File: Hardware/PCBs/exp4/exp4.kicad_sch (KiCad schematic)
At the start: 10 parts, among them J1 Conn_01x06_Female, J2 Conn_01x05_Female, J3 Conn_01x05_Female, J4 Conn_01x05_Female, U1 7486, U2 7486

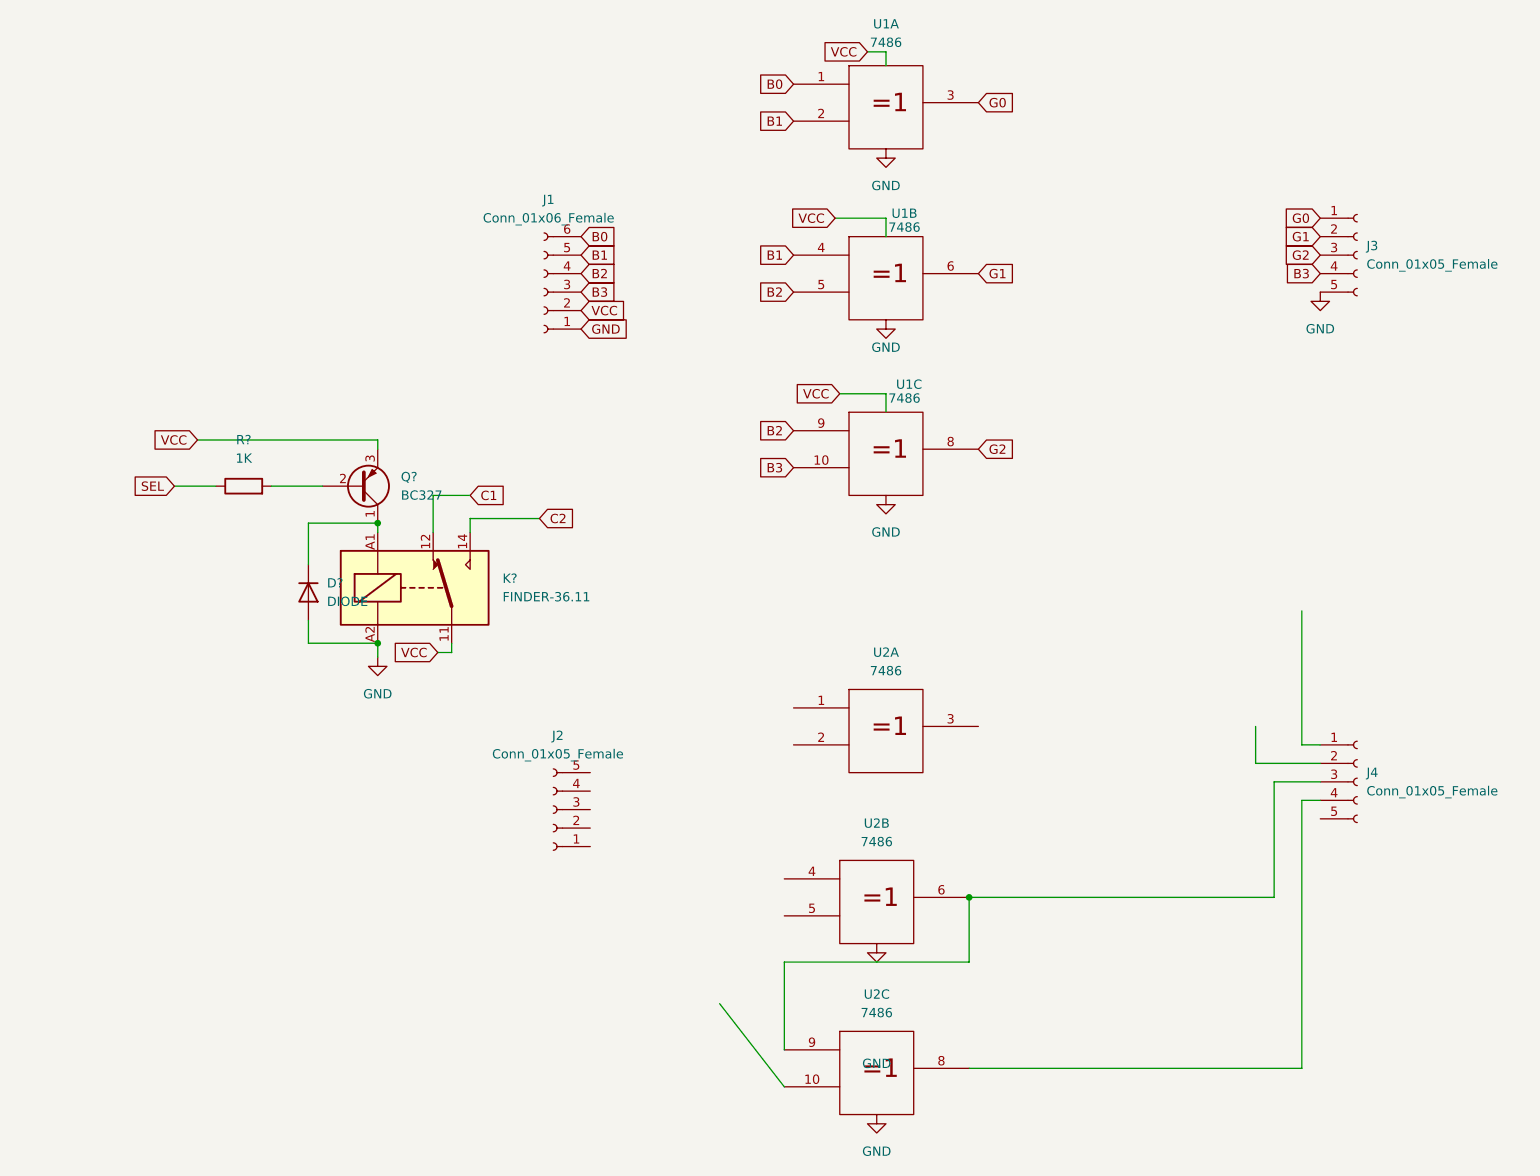
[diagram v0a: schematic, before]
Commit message: Several PCBs updated
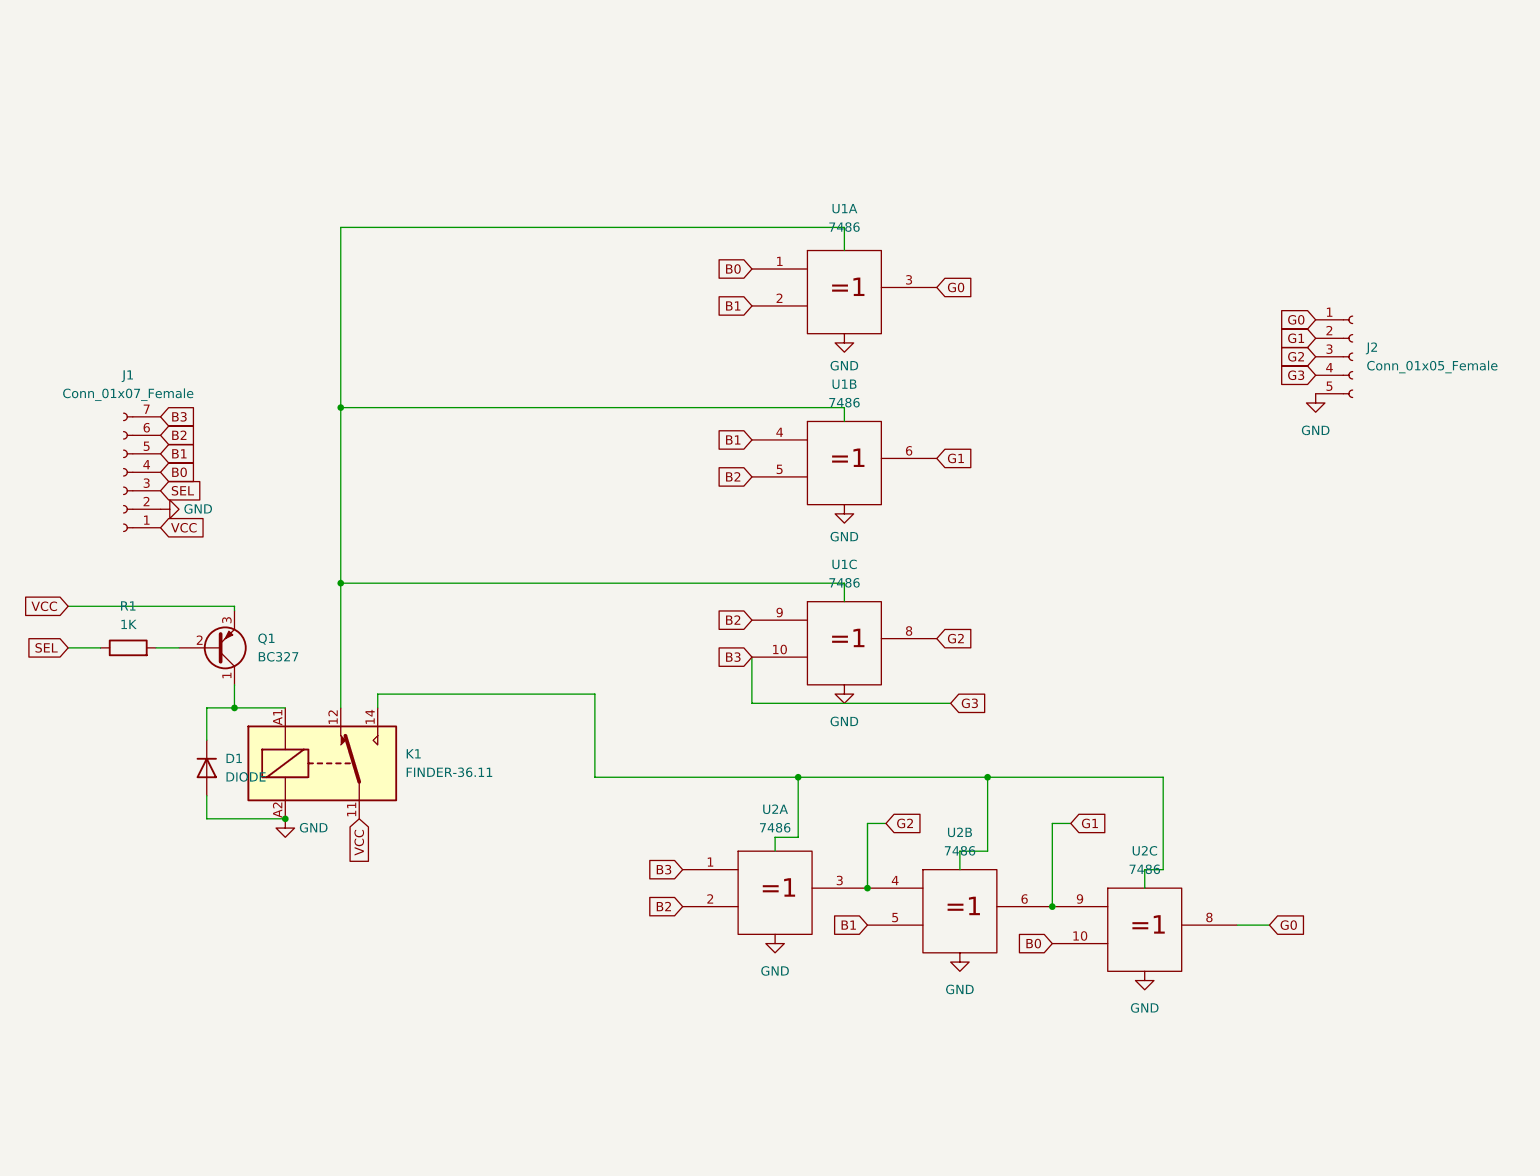
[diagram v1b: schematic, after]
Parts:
- removed D?: DIODE, Diode_SMD:D_MiniMELF, symbol Simulation_SPICE:DIODE
- removed J1: Conn_01x06_Female, Connector_JST:JST_EH_S6B-EH_1x06_P2.50mm_Horizontal, symbol Connector:Conn_01x06_Female
- removed J3, J4: Conn_01x05_Female, Connector_JST:JST_EH_S5B-EH_1x05_P2.50mm_Horizontal, symbol Connector:Conn_01x05_Female
- removed K?: FINDER-36.11, Relay_THT:Relay_SPDT_Finder_36.11, symbol Relay:FINDER-36.11
- removed Q?: BC327, Package_TO_SOT_THT:TO-92_Inline, symbol Transistor_BJT:BC327
- removed R?: 1K, Resistor_THT:R_Axial_DIN0207_L6.3mm_D2.5mm_P7.62mm_Horizontal, symbol Device:R
- added D1: DIODE, Diode_SMD:D_MiniMELF, symbol Simulation_SPICE:DIODE
- added J1: Conn_01x07_Female, Connector_JST:JST_EH_S7B-EH_1x07_P2.50mm_Horizontal, symbol Connector:Conn_01x07_Female
- added K1: FINDER-36.11, Relay_THT:Relay_SPDT_Finder_36.11, symbol Relay:FINDER-36.11
- added Q1: BC327, Package_TO_SOT_THT:TO-92_Inline, symbol Transistor_BJT:BC327
- added R1: 1K, Resistor_THT:R_Axial_DIN0207_L6.3mm_D2.5mm_P7.62mm_Horizontal, symbol Device:R
- U1, U2: footprint Package_DIP:DIP-14_W7.62mm -> Package_DIP:DIP-14_W7.62mm_Socket
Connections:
- net B0: now also U2.10, J1.4 (Pin_4)
- net B1: now also U2.5, J1.5 (Pin_5)
- net B2: now also U2.2, J1.6 (Pin_6)
- net B3: now also J2.4 (Pin_4), U2.1, J1.7 (Pin_7)
- net G0: now also J2.1 (Pin_1), U2.8
- net G1: now also J2.2 (Pin_2), U2.6, U2.9
- net G2: now also J2.3 (Pin_3), U2.3, U2.4
- net GND: now also J2.5 (Pin_5), D1.1 (A), J1.2 (Pin_2), K1.A2
- net SEL: now also J1.3 (Pin_3), R1.1
- net Vcc: now also K1.12, K1.14
- new net: D1.2 (K), K1.A1, Q1.1 (C)
- new net: Q1.2 (B), R1.2
- new net VCC: J1.1 (Pin_1), K1.11, Q1.3 (E)
